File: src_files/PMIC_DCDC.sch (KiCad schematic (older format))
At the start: 49 parts, among them U2 RK809

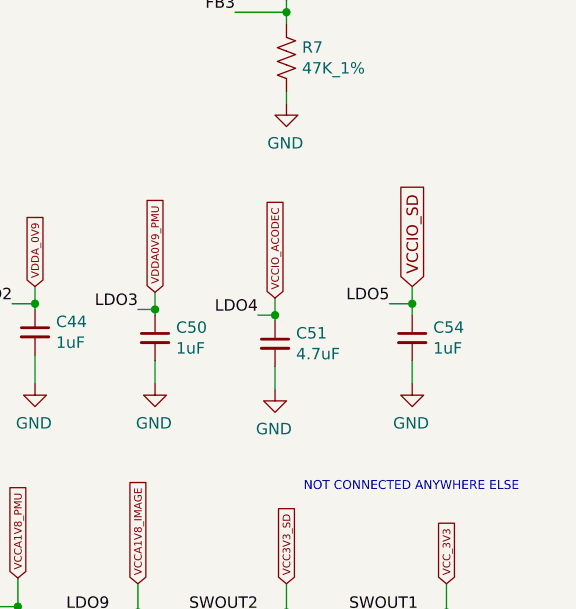
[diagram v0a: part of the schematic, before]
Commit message: complete update on schematic and all display interfaces
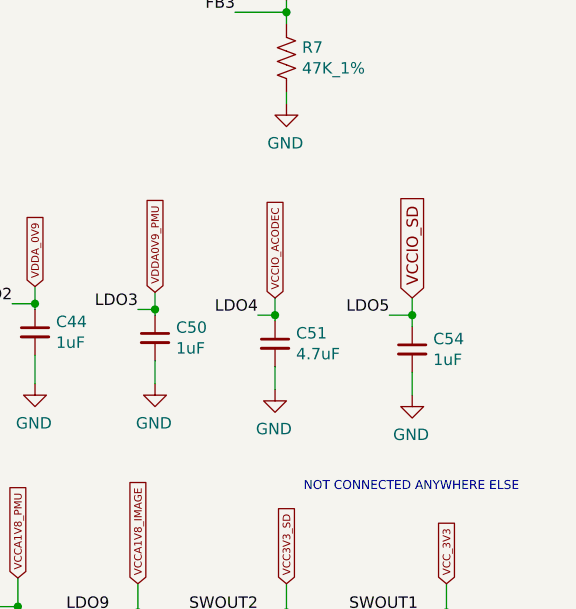
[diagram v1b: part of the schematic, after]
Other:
- moved on the sheet: C54
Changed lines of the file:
@@
 L Device:C_Small C54
 U 1 1 61F63EC5
-P 10650 4600
-F 0 "C54" H 10742 4646 50  0000 L CNN
-F 1 "1uF" H 10742 4555 50  0000 L CNN
-F 2 "Capacitor_SMD:C_0402_1005Metric" H 10650 4600 50  0001 C CNN
-F 3 "~" H 10650 4600 50  0001 C CNN
-	1    10650 4600
+P 10650 4650
+F 0 "C54" H 10742 4696 50  0000 L CNN
+F 1 "1uF" H 10742 4605 50  0000 L CNN
+F 2 "Capacitor_SMD:C_0402_1005Metric" H 10650 4650 50  0001 C CNN
+F 3 "~" H 10650 4650 50  0001 C CNN
+	1    10650 4650
 	1    0    0    -1
 $EndComp
@@
 L OLIMEX_Power:GND #PWR0149
 U 1 1 61F63ECF
-P 10650 4800
-F 0 "#PWR0149" H 10650 4550 50  0001 C CNN
-F 1 "GND" H 10655 4627 50  0000 C CNN
-F 2 "" H 10650 4800 60  0000 C CNN
-F 3 "" H 10650 4800 60  0000 C CNN
-	1    10650 4800
+P 10650 4850
+F 0 "#PWR0149" H 10650 4600 50  0001 C CNN
+F 1 "GND" H 10655 4677 50  0000 C CNN
+F 2 "" H 10650 4850 60  0000 C CNN
+F 3 "" H 10650 4850 60  0000 C CNN
+	1    10650 4850
 	-1   0    0    -1
 $EndComp
 Wire Wire Line
-	10650 4800 10650 4700
+	10650 4850 10650 4750
 $Comp
 L Device:C_Small C40
@@
 Wire Wire Line
 	8375 6175 8375 6075
-Text Label 10550 4450 2    50   ~ 0
+Text Label 10550 4500 2    50   ~ 0
 LDO5
 Text Label 7750 5800 2    50   ~ 0
@@
 Wire Wire Line
 	8925 6175 8925 6075
-Text GLabel 10650 4375 1    50   Input ~ 0
+Text GLabel 10650 4425 1    50   Input ~ 0
 VCCIO_SD
 Text GLabel 7850 5700 1    33   Input ~ 0
@@
 	9450 5675 9450 5800
 Wire Wire Line
-	10650 4375 10650 4450
+	10650 4425 10650 4500
 Wire Wire Line
-	10550 4450 10650 4450
-Connection ~ 10650 4450
+	10550 4500 10650 4500
+Connection ~ 10650 4500
 Wire Wire Line
-	10650 4450 10650 4500
+	10650 4500 10650 4550
 Wire Wire Line
 	7750 5800 7850 5800
